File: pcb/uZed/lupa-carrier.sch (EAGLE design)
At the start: 94 parts, among them J5 HDMI-TYPE-A-RECEPTICALFCI1002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, J6 HDMI-TYPE-A-RECEPTICALFCI1002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, K1 694108105102

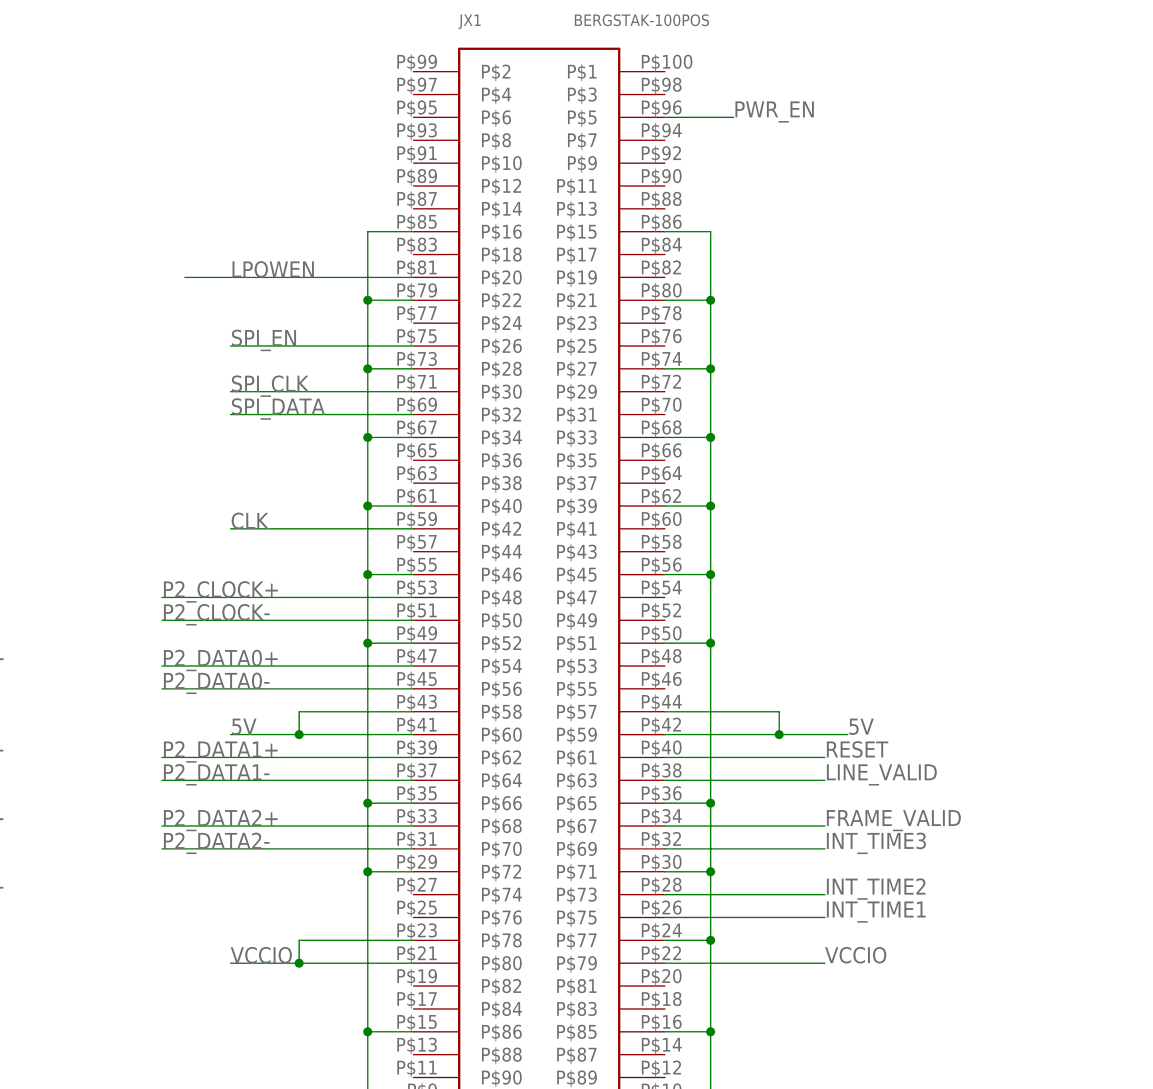
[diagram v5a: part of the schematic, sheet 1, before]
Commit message: lupa control signals routed
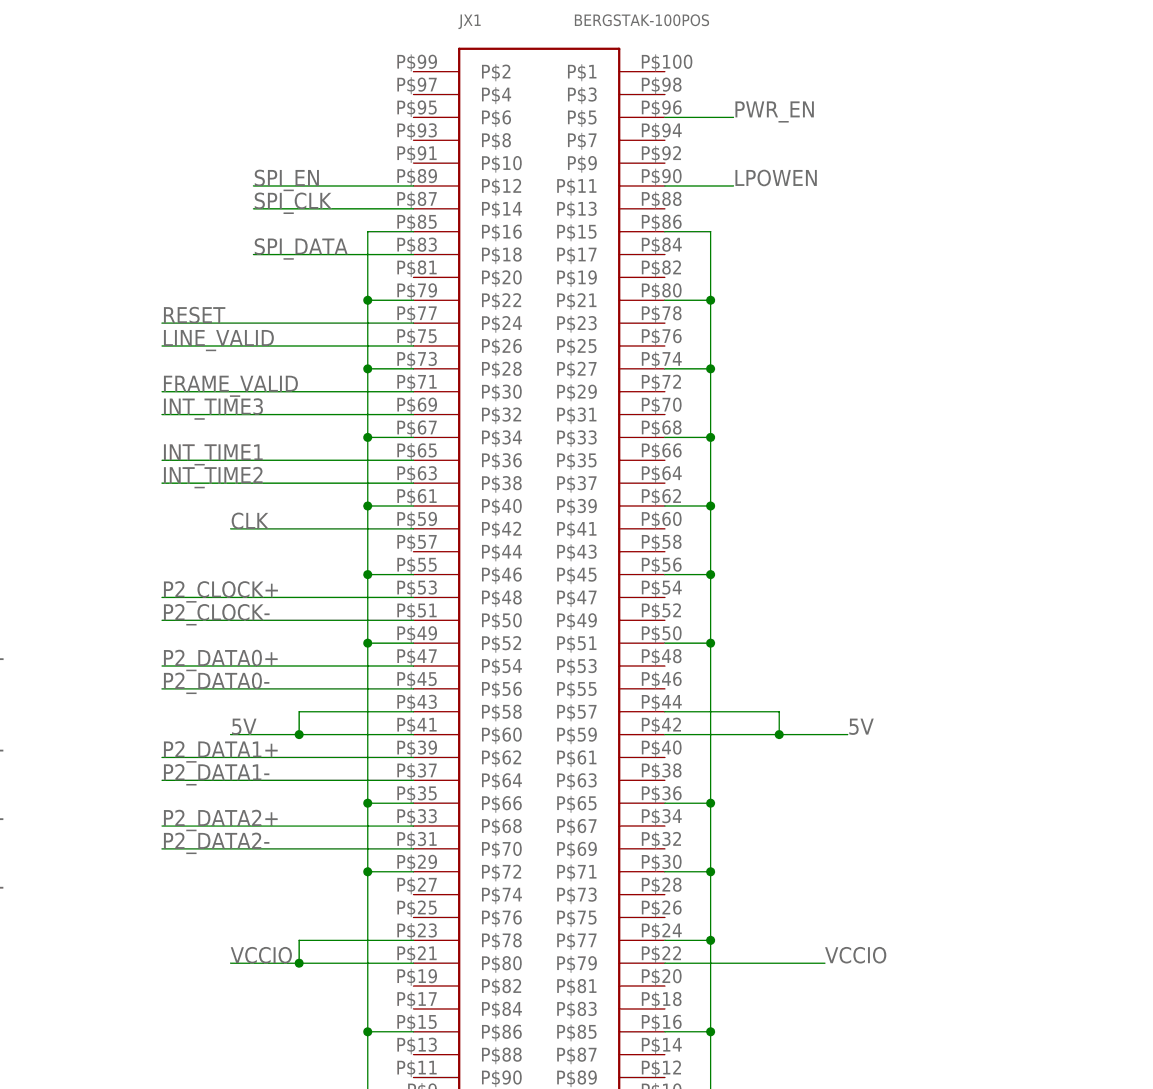
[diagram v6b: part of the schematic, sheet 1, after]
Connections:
- net FRAME_VALID: now also JX1.P$30; no longer JX1.P$67
- net INT_TIME1: now also JX1.P$36; no longer JX1.P$75
- net INT_TIME2: now also JX1.P$38; no longer JX1.P$73
- net INT_TIME3: now also JX1.P$32; no longer JX1.P$69
- net LINE_VALID: now also JX1.P$26; no longer JX1.P$63
- net LPOWEN: now also JX1.P$11; no longer JX1.P$20
- net RESET: now also JX1.P$24; no longer JX1.P$61
- net SPI_CLK: now also JX1.P$14; no longer JX1.P$30
- net SPI_DATA: now also JX1.P$18; no longer JX1.P$32
- net SPI_EN: now also JX1.P$12; no longer JX1.P$26
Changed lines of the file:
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@@
 <net name="SPI_DATA" class="0">
 <segment>
+<pinref part="JX1" gate="G$1" pin="P$18"/>
+<wire x1="142.24" y1="129.54" x2="124.46" y2="129.54" width="0.1524" layer="91"/>
+<label x="124.46" y="129.54" size="1.778" layer="95"/>
+</segment>
+</net>
+<net name="SPI_CLK" class="0">
+<segment>
+<pinref part="JX1" gate="G$1" pin="P$14"/>
+<wire x1="142.24" y1="134.62" x2="124.46" y2="134.62" width="0.1524" layer="91"/>
+<label x="124.46" y="134.62" size="1.778" layer="95"/>
+</segment>
+</net>
+<net name="LINE_VALID" class="0">
+<segment>
+<pinref part="JX1" gate="G$1" pin="P$26"/>
+<wire x1="142.24" y1="119.38" x2="114.3" y2="119.38" width="0.1524" layer="91"/>
+<label x="114.3" y="119.38" size="1.778" layer="95"/>
+</segment>
+</net>
+<net name="FRAME_VALID" class="0">
+<segment>
+<pinref part="JX1" gate="G$1" pin="P$30"/>
+<wire x1="142.24" y1="114.3" x2="114.3" y2="114.3" width="0.1524" layer="91"/>
+<label x="114.3" y="114.3" size="1.778" layer="95"/>
+</segment>
+</net>
+<net name="RESET" class="0">
+<segment>
+<pinref part="JX1" gate="G$1" pin="P$24"/>
+<wire x1="142.24" y1="121.92" x2="114.3" y2="121.92" width="0.1524" layer="91"/>
+<label x="114.3" y="121.92" size="1.778" layer="95"/>
+</segment>
+</net>
+<net name="INT_TIME3" class="0">
+<segment>
 <pinref part="JX1" gate="G$1" pin="P$32"/>
-<wire x1="142.24" y1="111.76" x2="121.92" y2="111.76" width="0.1524" layer="91"/>
-<label x="121.92" y="111.76" size="1.778" layer="95"/>
-</segment>
-</net>
-<net name="SPI_CLK" class="0">
-<segment>
-<pinref part="JX1" gate="G$1" pin="P$30"/>
-<wire x1="142.24" y1="114.3" x2="121.92" y2="114.3" width="0.1524" layer="91"/>
-<label x="121.92" y="114.3" size="1.778" layer="95"/>
-</segment>
-</net>
-<net name="SPI_EN" class="0">
-<segment>
-<pinref part="JX1" gate="G$1" pin="P$26"/>
-<wire x1="142.24" y1="119.38" x2="121.92" y2="119.38" width="0.1524" layer="91"/>
-<label x="121.92" y="119.38" size="1.778" layer="95"/>
-</segment>
-</net>
-<net name="LINE_VALID" class="0">
-<segment>
-<pinref part="JX1" gate="G$1" pin="P$63"/>
-<wire x1="170.18" y1="71.12" x2="187.96" y2="71.12" width="0.1524" layer="91"/>
-<label x="187.96" y="71.12" size="1.778" layer="95"/>
-</segment>
-</net>
-<net name="FRAME_VALID" class="0">
-<segment>
-<pinref part="JX1" gate="G$1" pin="P$67"/>
-<wire x1="170.18" y1="66.04" x2="187.96" y2="66.04" width="0.1524" layer="91"/>
-<label x="187.96" y="66.04" size="1.778" layer="95"/>
-</segment>
-</net>
-<net name="RESET" class="0">
-<segment>
-<pinref part="JX1" gate="G$1" pin="P$61"/>
-<wire x1="170.18" y1="73.66" x2="187.96" y2="73.66" width="0.1524" layer="91"/>
-<label x="187.96" y="73.66" size="1.778" layer="95"/>
-</segment>
-</net>
-<net name="INT_TIME3" class="0">
-<segment>
-<pinref part="JX1" gate="G$1" pin="P$69"/>
-<wire x1="170.18" y1="63.5" x2="187.96" y2="63.5" width="0.1524" layer="91"/>
-<label x="187.96" y="63.5" size="1.778" layer="95"/>
-</segment>
-</net>
-<net name="INT_TIME2" class="0">
-<segment>
-<pinref part="JX1" gate="G$1" pin="P$73"/>
-<wire x1="170.18" y1="58.42" x2="187.96" y2="58.42" width="0.1524" layer="91"/>
-<label x="187.96" y="58.42" size="1.778" layer="95"/>
-</segment>
-</net>
-<net name="INT_TIME1" class="0">
-<segment>
-<pinref part="JX1" gate="G$1" pin="P$75"/>
-<wire x1="170.18" y1="55.88" x2="187.96" y2="55.88" width="0.1524" layer="91"/>
-<label x="187.96" y="55.88" size="1.778" layer="95"/>
-</segment>
-</net>
-<net name="LPOWEN" class="0">
-<segment>
-<pinref part="JX1" gate="G$1" pin="P$20"/>
-<wire x1="142.24" y1="127" x2="116.84" y2="127" width="0.1524" layer="91"/>
-<label x="121.92" y="127" size="1.778" layer="95"/>
+<wire x1="142.24" y1="111.76" x2="114.3" y2="111.76" width="0.1524" layer="91"/>
+<label x="114.3" y="111.76" size="1.778" layer="95"/>
 </segment>
 </net>
@@
 <wire x1="63.5" y1="55.88" x2="83.82" y2="55.88" width="0.1524" layer="91"/>
 <label x="83.82" y="55.88" size="1.778" layer="95"/>
+</segment>
+</net>
+<net name="LPOWEN" class="0">
+<segment>
+<pinref part="JX1" gate="G$1" pin="P$11"/>
+<wire x1="170.18" y1="137.16" x2="177.8" y2="137.16" width="0.1524" layer="91"/>
+<label x="177.8" y="137.16" size="1.778" layer="95"/>
+</segment>
+</net>
+<net name="SPI_EN" class="0">
+<segment>
+<pinref part="JX1" gate="G$1" pin="P$12"/>
+<wire x1="142.24" y1="137.16" x2="124.46" y2="137.16" width="0.1524" layer="91"/>
+<label x="124.46" y="137.16" size="1.778" layer="95"/>
+</segment>
+</net>
+<net name="INT_TIME1" class="0">
+<segment>
+<pinref part="JX1" gate="G$1" pin="P$36"/>
+<wire x1="142.24" y1="106.68" x2="114.3" y2="106.68" width="0.1524" layer="91"/>
+<label x="114.3" y="106.68" size="1.778" layer="95"/>
+</segment>
+</net>
+<net name="INT_TIME2" class="0">
+<segment>
+<pinref part="JX1" gate="G$1" pin="P$38"/>
+<wire x1="142.24" y1="104.14" x2="114.3" y2="104.14" width="0.1524" layer="91"/>
+<label x="114.3" y="104.14" size="1.778" layer="95"/>
 </segment>
 </net>
@@
 <net name="VDDA" class="0">
 <segment>
-<pinref part="U$4" gate="G$1" pin="VDDA"/>
-<wire x1="60.96" y1="91.44" x2="53.34" y2="91.44" width="0.1524" layer="91"/>
-<label x="48.26" y="91.44" size="1.778" layer="95"/>
-</segment>
-<segment>
-<pinref part="U$4" gate="G$1" pin="VDDA1"/>
-<wire x1="152.4" y1="81.28" x2="160.02" y2="81.28" width="0.1524" layer="91"/>
-<label x="165.1" y="81.28" size="1.778" layer="95" rot="R180"/>
-</segment>
-<segment>
 <pinref part="R25" gate="G$1" pin="2"/>
 <wire x1="254" y1="139.7" x2="254" y2="142.24" width="0.1524" layer="91"/>
@@
 <wire x1="256.54" y1="73.66" x2="256.54" y2="76.2" width="0.1524" layer="91"/>
 <label x="256.54" y="76.2" size="1.778" layer="95"/>
+</segment>
+<segment>
+<pinref part="U$4" gate="G$1" pin="VDDA1"/>
+<wire x1="152.4" y1="81.28" x2="162.56" y2="81.28" width="0.1524" layer="91"/>
+<label x="157.48" y="81.28" size="1.778" layer="95"/>
+</segment>
+<segment>
+<pinref part="U$4" gate="G$1" pin="VDDA"/>
+<wire x1="60.96" y1="91.44" x2="48.26" y2="91.44" width="0.1524" layer="91"/>
+<label x="48.26" y="91.44" size="1.778" layer="95"/>
 </segment>
 </net>
@@
 <segment>
 <pinref part="F2" gate="G$1" pin="1"/>
+<pinref part="C5" gate="G$1" pin="1"/>
 <wire x1="55.88" y1="33.02" x2="50.8" y2="33.02" width="0.1524" layer="91"/>
-<pinref part="C5" gate="G$1" pin="1"/>
-<wire x1="50.8" y1="33.02" x2="40.64" y2="33.02" width="0.1524" layer="91"/>
 <wire x1="50.8" y1="30.48" x2="50.8" y2="33.02" width="0.1524" layer="91"/>
-<junction x="50.8" y="33.02"/>
-<label x="40.64" y="33.02" size="1.778" layer="95"/>
-</segment>
-</net>
+<wire x1="50.8" y1="33.02" x2="43.18" y2="33.02" width="0.1524" layer="91"/>
+<label x="43.18" y="33.02" size="1.778" layer="95"/>
+</segment>
+</net>

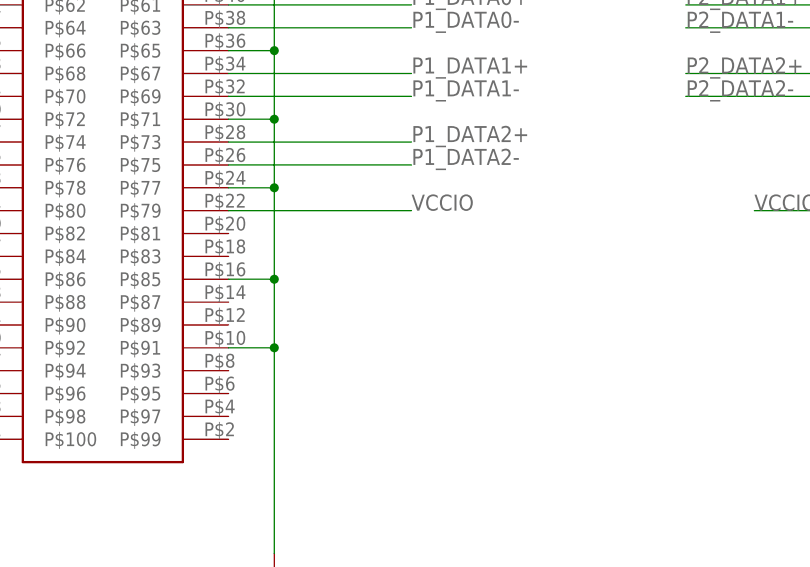
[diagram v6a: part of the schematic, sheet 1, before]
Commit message: finished component layout
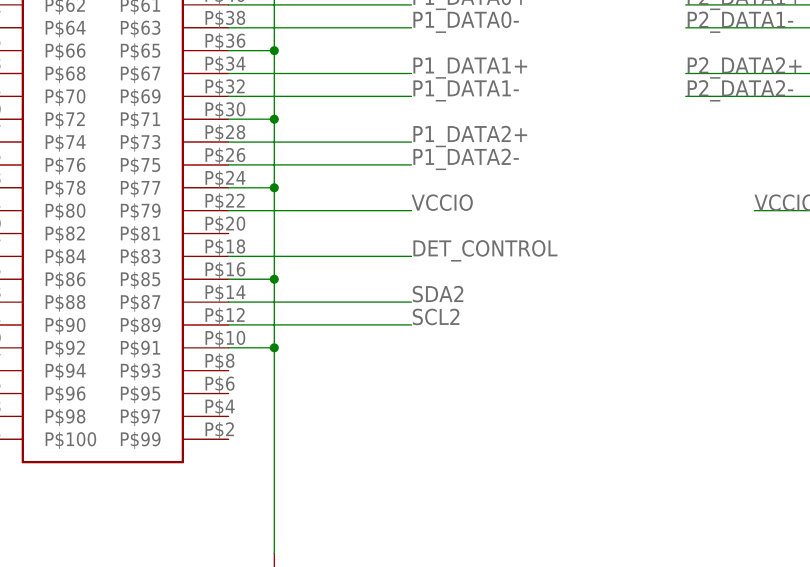
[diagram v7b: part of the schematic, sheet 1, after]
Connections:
- net DET_CONTROL: now also JX2.P$83
- net SCL2: now also JX2.P$89
- net SDA2: now also JX2.P$87
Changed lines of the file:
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@@
+</segment>
+</net>
+<net name="SDA2" class="0">
+<segment>
+<pinref part="JX2" gate="G$1" pin="P$87"/>
+<wire x1="63.5" y1="40.64" x2="83.82" y2="40.64" width="0.1524" layer="91"/>
+<label x="83.82" y="40.64" size="1.778" layer="95"/>
+</segment>
+</net>
+<net name="SCL2" class="0">
+<segment>
+<pinref part="JX2" gate="G$1" pin="P$89"/>
+<wire x1="63.5" y1="38.1" x2="83.82" y2="38.1" width="0.1524" layer="91"/>
+<label x="83.82" y="38.1" size="1.778" layer="95"/>
+</segment>
+</net>
+<net name="DET_CONTROL" class="0">
+<segment>
+<pinref part="JX2" gate="G$1" pin="P$83"/>
+<wire x1="63.5" y1="45.72" x2="83.82" y2="45.72" width="0.1524" layer="91"/>
+<label x="83.82" y="45.72" size="1.778" layer="95"/>
 </segment>
 </net>
